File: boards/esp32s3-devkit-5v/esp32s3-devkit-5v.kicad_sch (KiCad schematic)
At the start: 74 parts, among them J1 Conn_01x02_Pin, J2 USB_C_Receptacle_USB2.0_16P, J3 Conn_01x02_Pin, J4 Conn_01x04_Pin, Q1 AO3401A, Q2 AO3401A, Q3 MMBT3904, SW1 MK-12C03-G015, SW2 RESET, SW3 BOOT, SW4 MODE, SW5 VOL_UP, SW6 VOL_DOWN, SW7 BTN4, U1 TPS63070RNMR, U2 TPS63070RNMR, U3 ESP32-S3-WROOM-1-N16, U4 USBLC6-2SC6, U5 RV-3028-C7, U6 MAX98357A

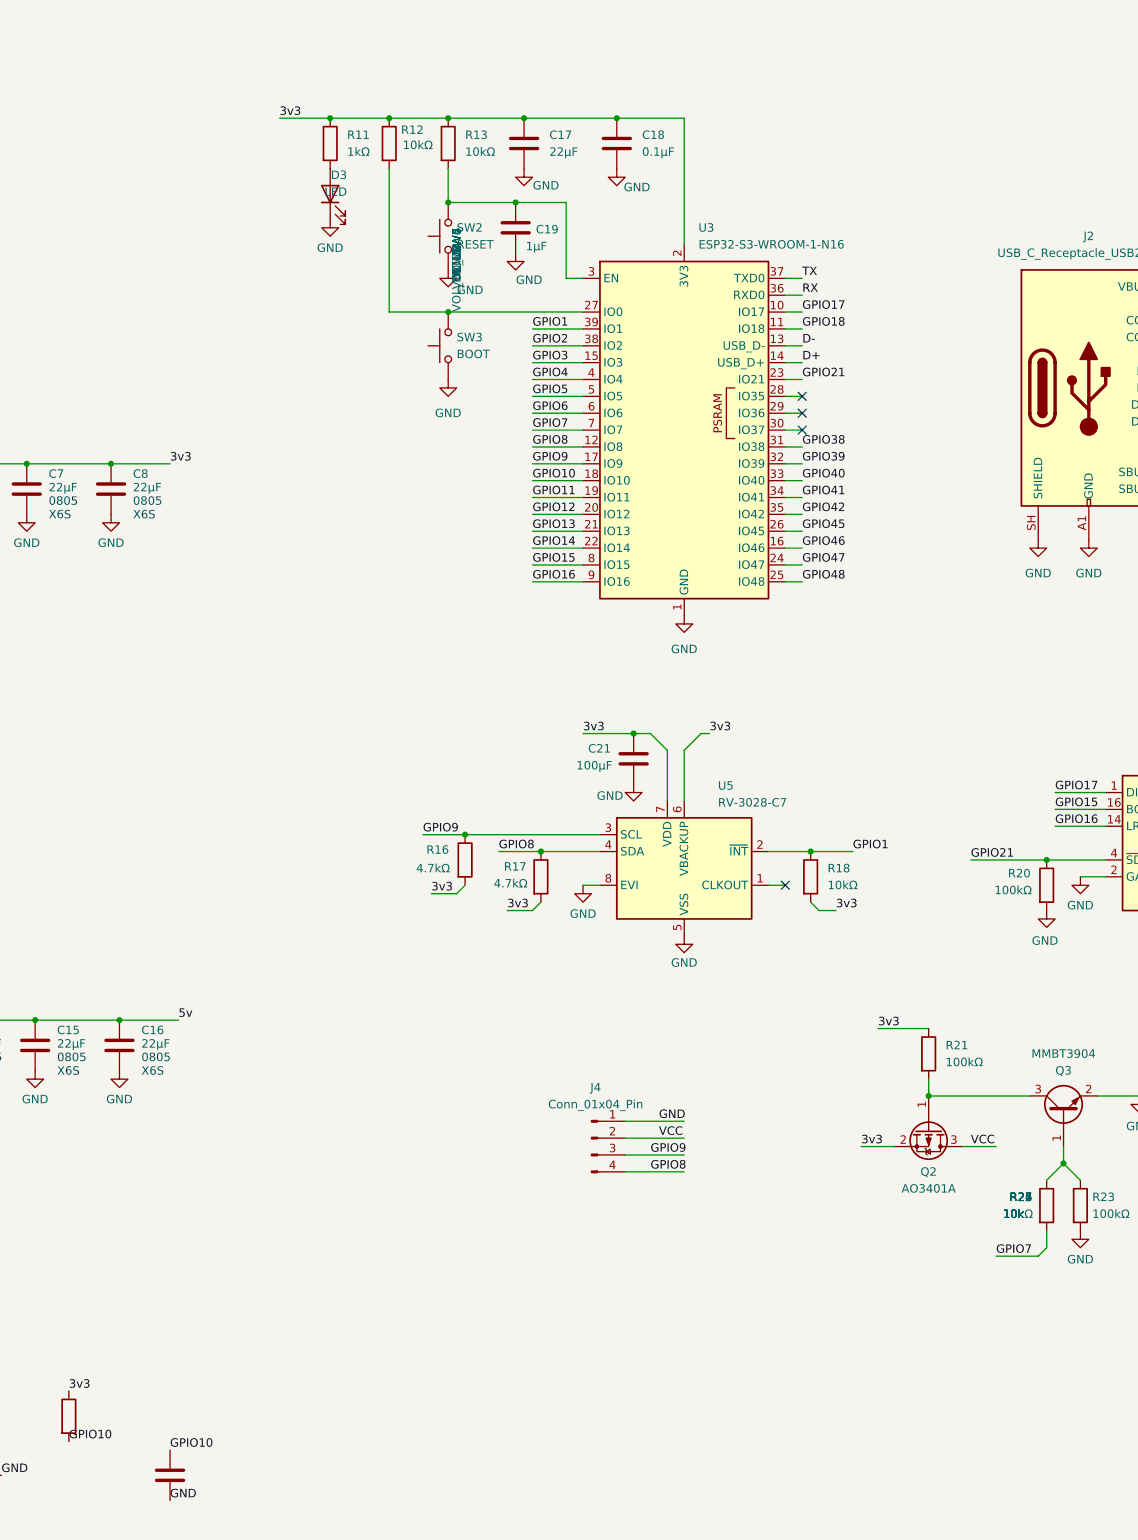
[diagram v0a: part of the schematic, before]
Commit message: feat(esp32s3-devkit-5v): add RGB status LED (D4, common cathode)
Device:LED_RGBK on GPIO38/39/40 (PWM via LEDC), cathode to GND:
  GPIO38 -[R28 330R]- red anode
  GPIO39 -[R29 150R]- green anode
  GPIO40 -[R30 150R]- blue anode

Runs native at 3.3V (deliberately NOT the gated 5V rail, which is off outside
alarm sessions). Green/blue get smaller resistors because their ~3.0-3.2V Vf
leaves little headroom at 3.3V - they run dimmer than red; fine for a status
indicator. Footprint: Wuerth PLCC4 3.2x2.8mm (pads 1-4 match symbol pins);
confirm the final LCSC part is common-cathode with the same pinout at BOM time.

lib-symbol Device:LED_RGBK imported from KiCad's Device library; instance
added via kicad-skip with grid-aligned label connectivity like the buttons.

Firmware TODO (cube_browns.ino): define the three LEDC channels on 38/39/40.

Co-Authored-By: Claude Opus 4.8 <noreply@anthropic.com>
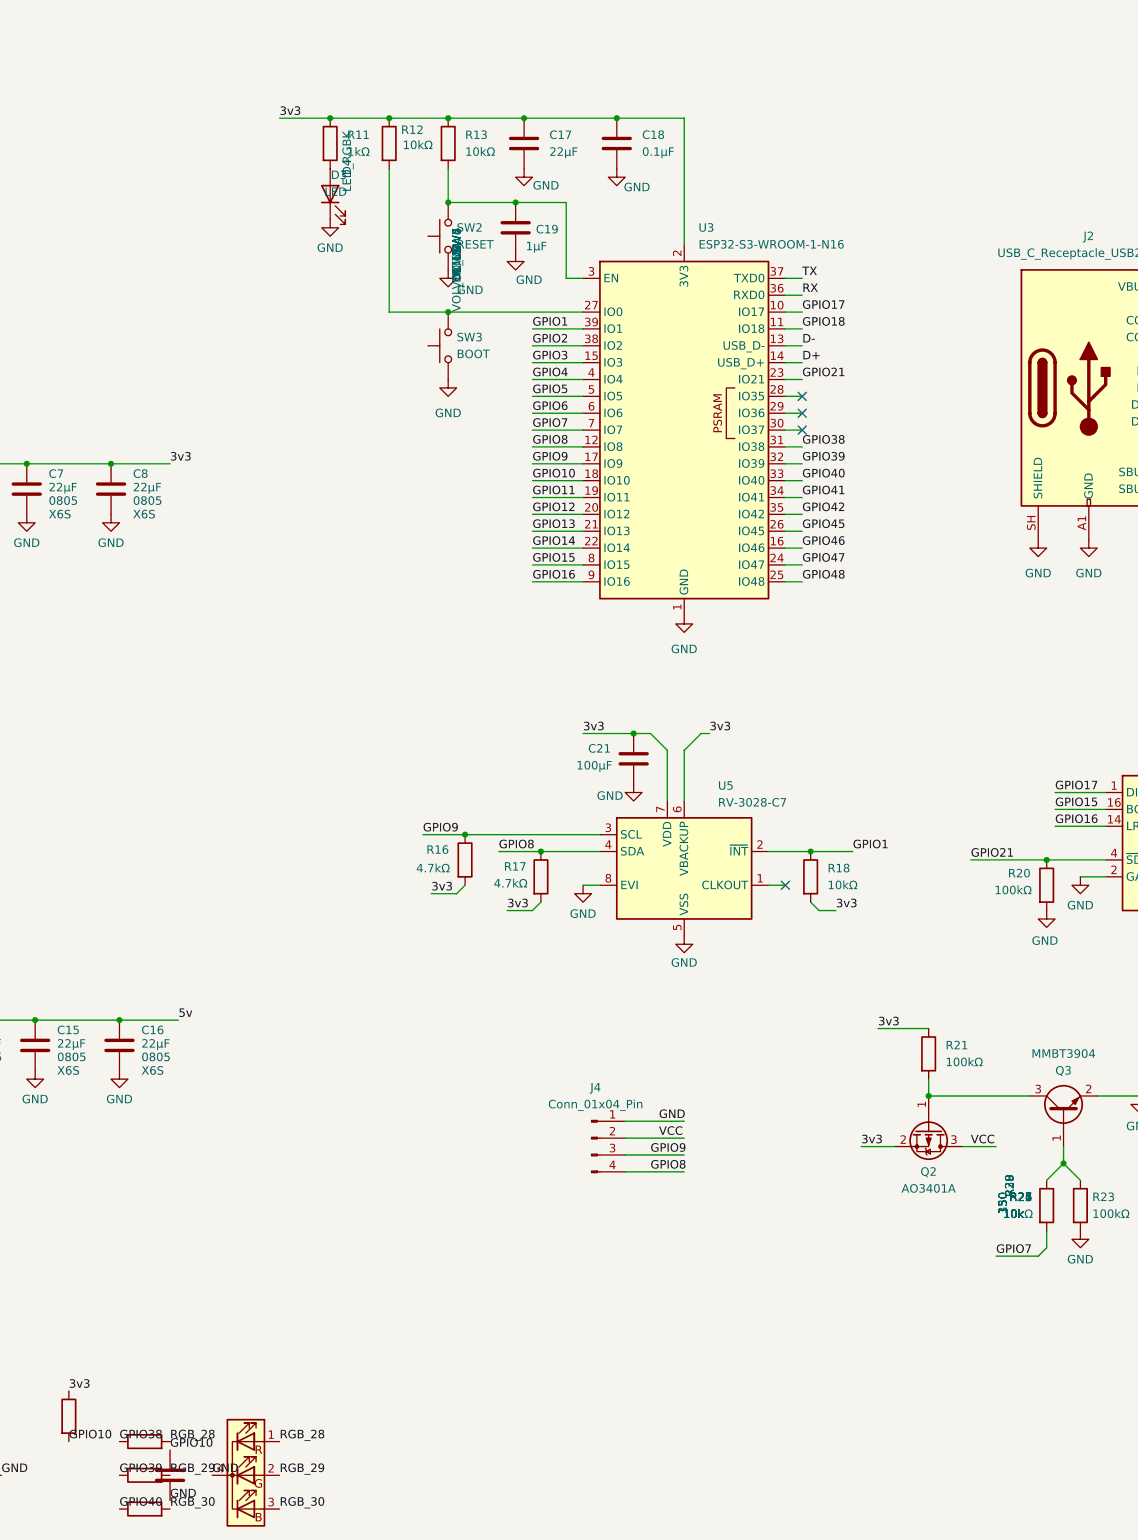
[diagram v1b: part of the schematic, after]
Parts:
- added D4: LED_RGBK, LED_SMD:LED_RGB_Wuerth-PLCC4_3.2x2.8mm_150141M173100, symbol Device:LED_RGBK
- added R28: 330, symbol Device:R
- added R29, R30: 150, symbol Device:R
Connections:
- net GND: now also D4.4 (K)
- net GPIO38: now also R28.1
- net GPIO39: now also R29.1
- net GPIO40: now also R30.1
- new net RGB_28: D4.1 (RA), R28.2
- new net RGB_29: D4.2 (GA), R29.2
- new net RGB_30: D4.3 (BA), R30.2

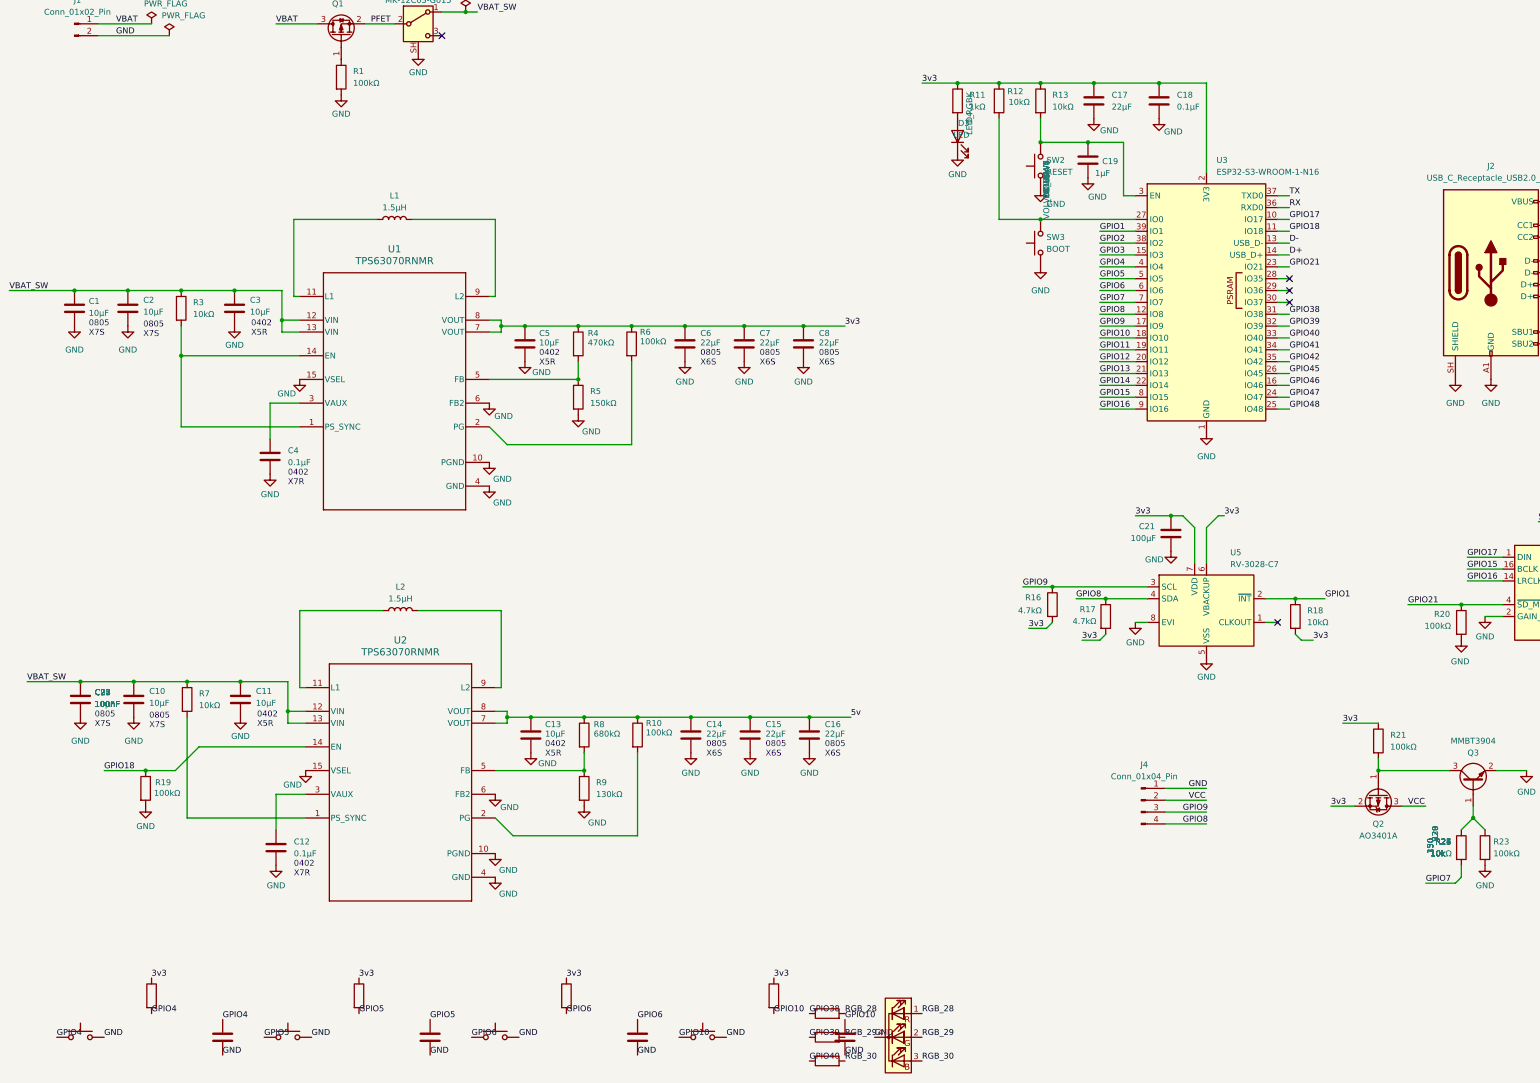
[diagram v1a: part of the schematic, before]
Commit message: revert: remove generated buttons + RGB LED from esp32s3-devkit-5v
Restores the schematic to 6b672a7 (last fully hand-drawn state: amp + display).
The programmatically-added front-panel parts were electrically correct but
visually disorganized — Erik will redraw them by hand from the wiring spec:

- 4 buttons: SW->GPIO node + GND, 10k pull-up node->3v3, 100nF node->GND,
  on GPIO4 (MODE), GPIO5 (VOL_UP), GPIO6 (VOL_DOWN), GPIO10 (BTN4)
- RGB LED (Device:LED_RGBK, common cathode): GPIO38-[330R]-RA, GPIO39-[150R]-GA,
  GPIO40-[150R]-BA, K->GND; fp LED_SMD:LED_RGB_Wuerth-PLCC4_3.2x2.8mm

Co-Authored-By: Claude Opus 4.8 <noreply@anthropic.com>
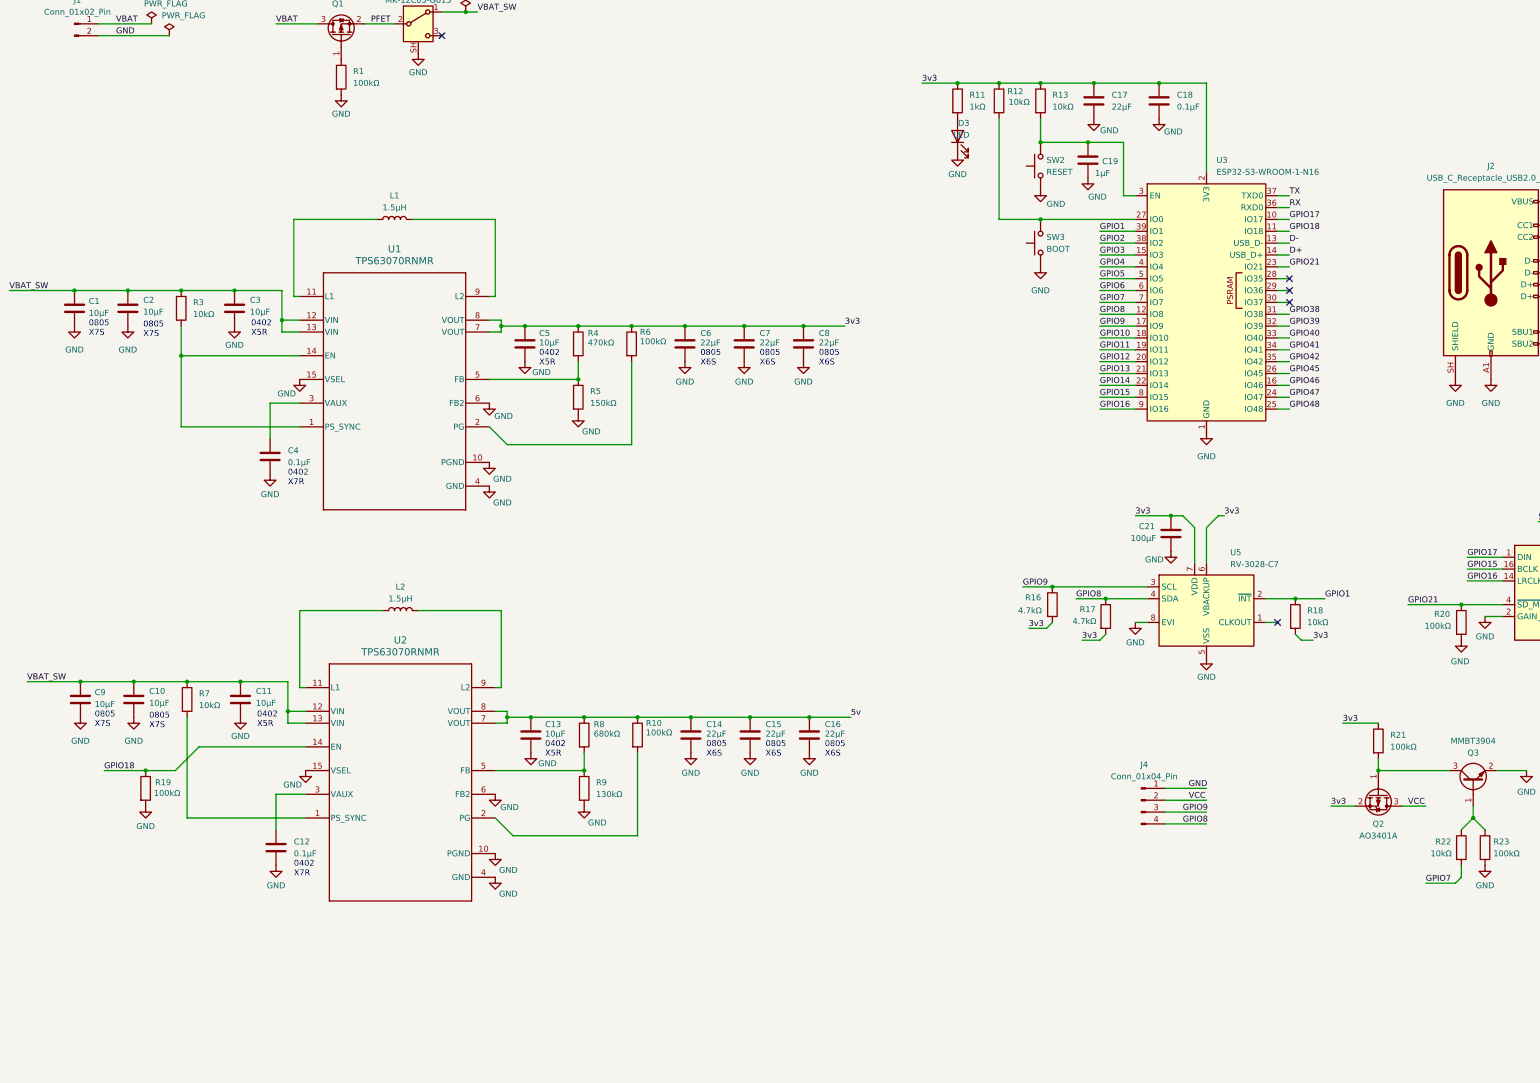
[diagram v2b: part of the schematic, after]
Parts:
- removed C22, C23, C24, C25: 100nF, Capacitor_SMD:C_0805_2012Metric, symbol Device:C
- removed D4: LED_RGBK, LED_SMD:LED_RGB_Wuerth-PLCC4_3.2x2.8mm_150141M173100, symbol Device:LED_RGBK
- removed R24, R25, R26, R27: 10k, symbol Device:R
- removed R28: 330, symbol Device:R
- removed R29, R30: 150, symbol Device:R
- removed SW4: MODE, Button_Switch_SMD:SW_Push_1P1T_XKB_TS-1187A, symbol Switch:SW_Push
- removed SW5: VOL_UP, Button_Switch_SMD:SW_Push_1P1T_XKB_TS-1187A, symbol Switch:SW_Push
- removed SW6: VOL_DOWN, Button_Switch_SMD:SW_Push_1P1T_XKB_TS-1187A, symbol Switch:SW_Push
- removed SW7: BTN4, Button_Switch_SMD:SW_Push_1P1T_XKB_TS-1187A, symbol Switch:SW_Push
